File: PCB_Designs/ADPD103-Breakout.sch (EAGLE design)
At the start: 3 parts

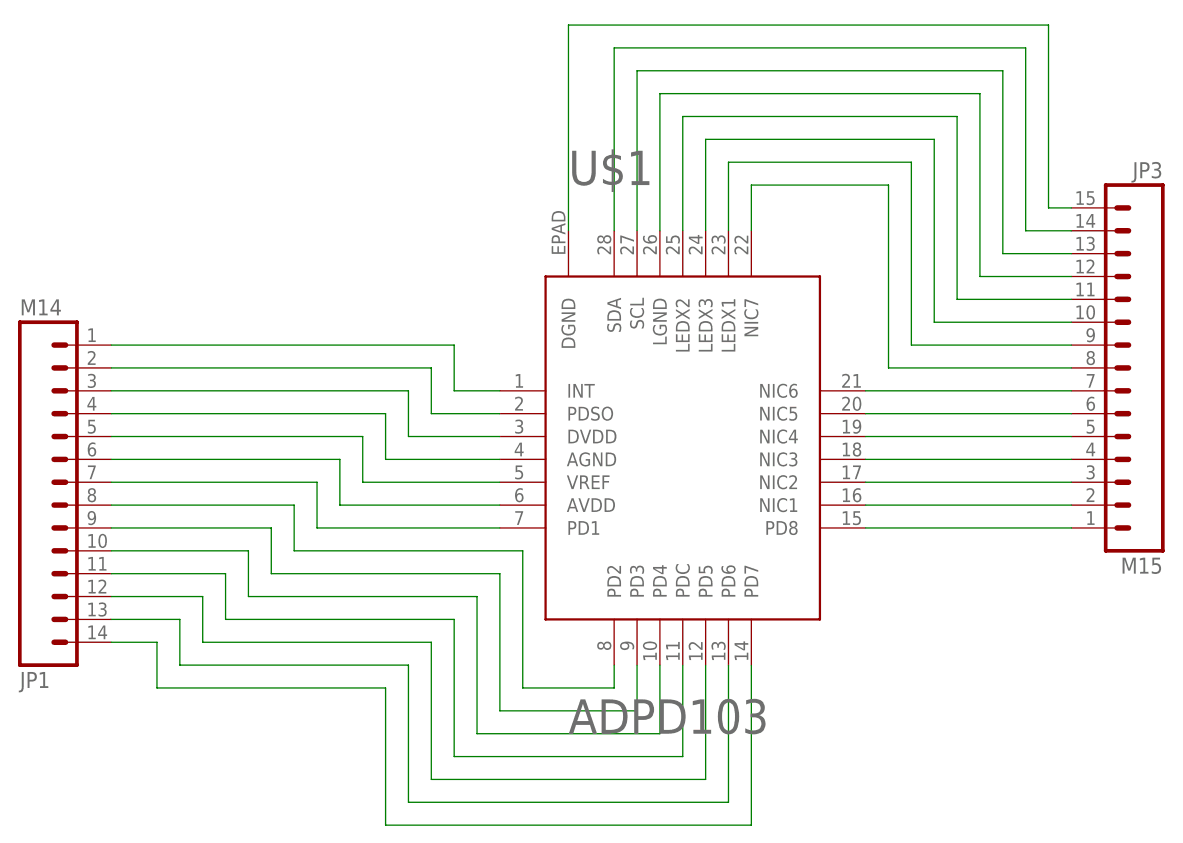
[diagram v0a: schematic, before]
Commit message: first order sent to OSHPark
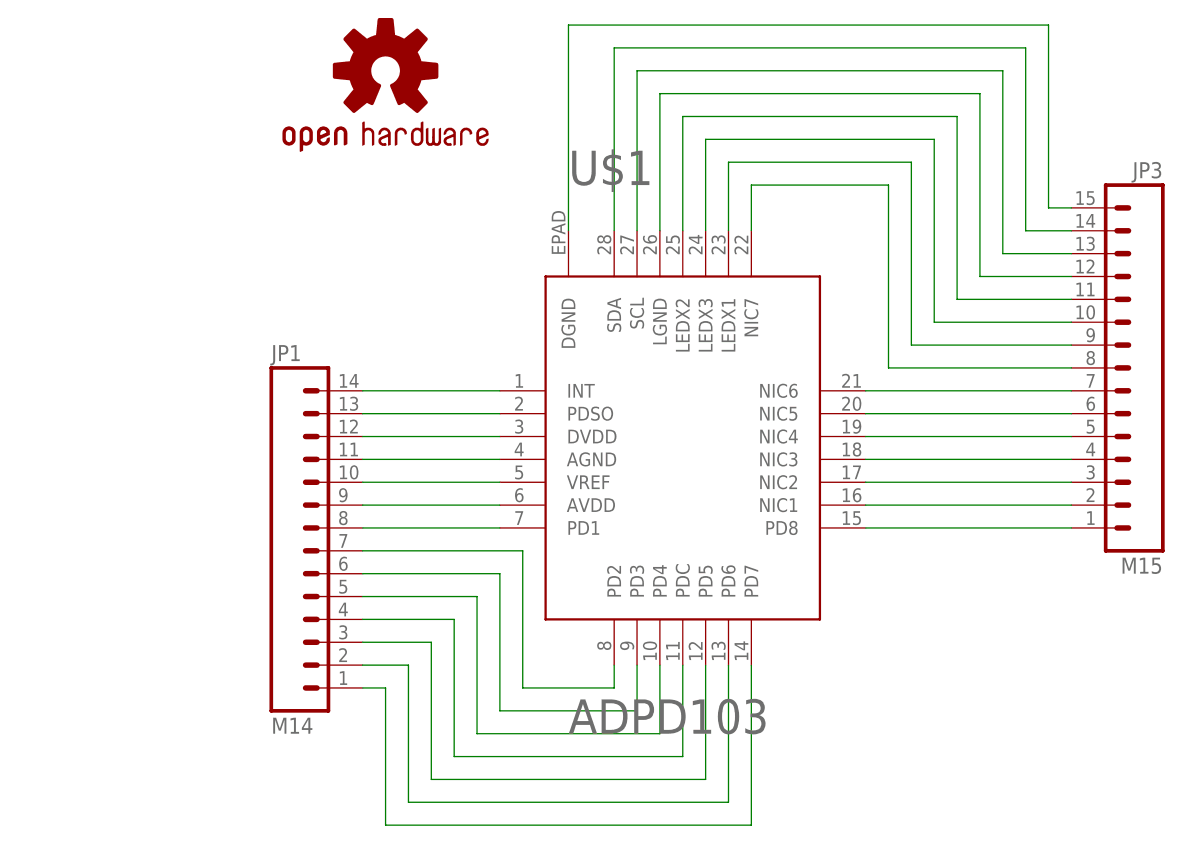
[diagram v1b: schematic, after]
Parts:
- added LOGO1: OSHW-LOGOS, SparkFun-Aesthetics:OSHW-LOGOS
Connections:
- net N$1: now also JP1.14; no longer JP1.1
- net N$10: now also JP1.5; no longer JP1.10
- net N$11: now also JP1.4; no longer JP1.11
- net N$12: now also JP1.3; no longer JP1.12
- net N$13: now also JP1.2; no longer JP1.13
- net N$14: now also JP1.1; no longer JP1.14
- net N$2: now also JP1.13; no longer JP1.2
- net N$3: now also JP1.12; no longer JP1.3
- net N$4: now also JP1.11; no longer JP1.4
- net N$5: now also JP1.10; no longer JP1.5
- net N$6: now also JP1.9; no longer JP1.6
- net N$7: now also JP1.8; no longer JP1.7
- net N$8: now also JP1.7; no longer JP1.8
- net N$9: now also JP1.6; no longer JP1.9
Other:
- note added: "Creative Commons License Attribution-NonCommercial- ShareAlike 3.0 Unported"
- note added: "Orlando S. Hoilett CalvaryEng, IICEPD ADPD103 Breakout"
- moved on the sheet: JP1
